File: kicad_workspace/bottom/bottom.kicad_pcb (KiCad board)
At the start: 4 copper layers, 76.8 x 84 mm, 75 parts, among them J1 691103110002, J2 BackupPad, J3 PROG_HEADER, J4 RPI_POWER_CONN, J5 UART_HEADER, J6 BackupPad, M1 N20_MOTOR_EXTENDED_SHAFT, M2 N20_MOTOR_EXTENDED_SHAFT, U1 DRV8833PWP, U12 ACS712-5A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

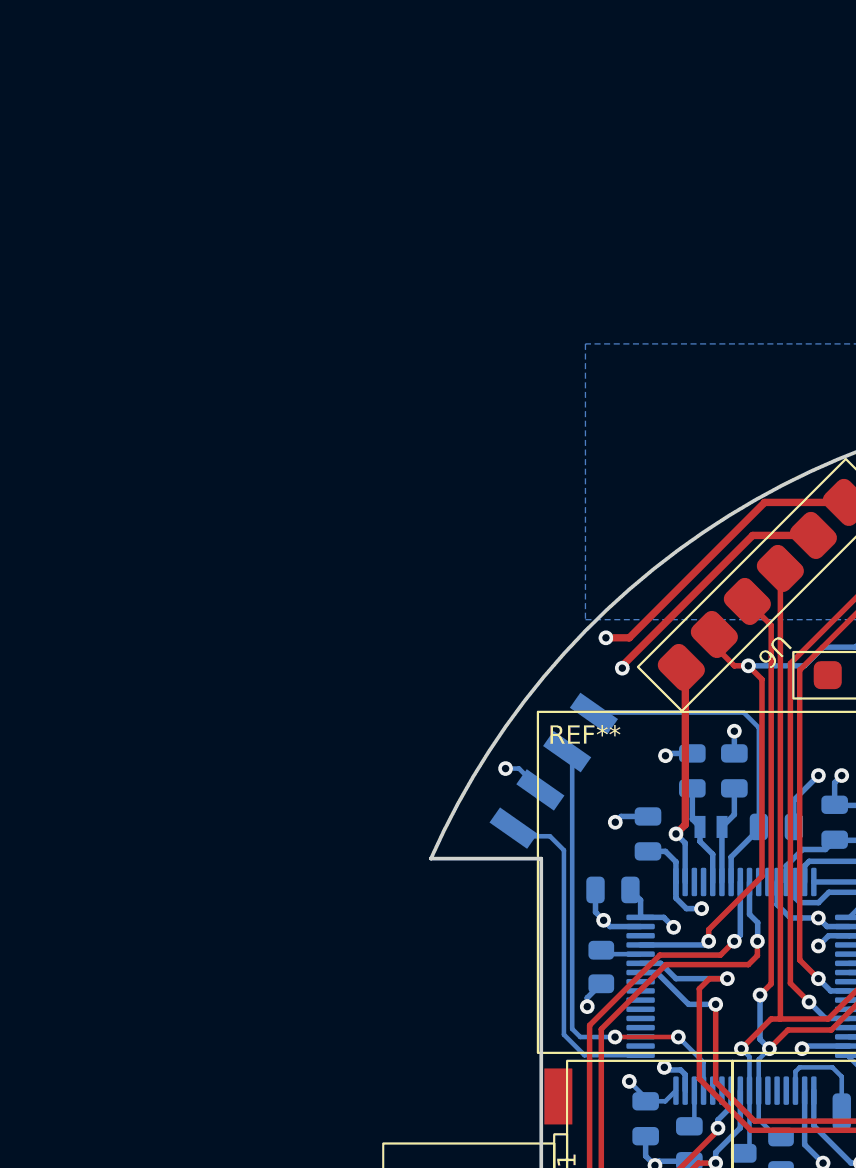
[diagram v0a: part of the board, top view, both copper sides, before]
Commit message: add 3.3v to programming header
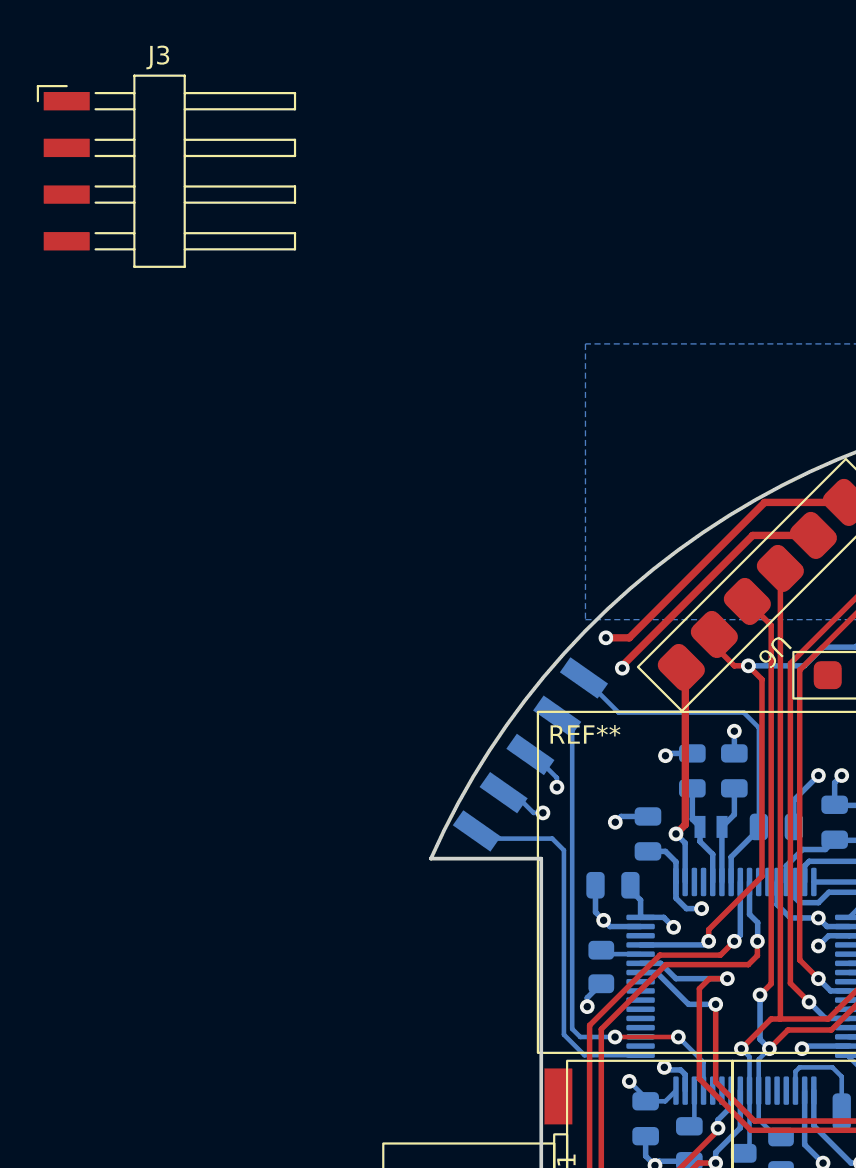
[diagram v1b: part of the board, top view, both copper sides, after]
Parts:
- added J7: Conn_01x05_Pin, Connector_Harwin:Harwin_M20-89005xx_1x05_P2.54mm_Horizontal, B.Cu at (22.5, 34.2)
- J3: moved to F.Cu
- moved J3 33.7 mm to (7.30, 5.61), turned to 0 degrees
- moved C11 0.25 mm to (31.5, 44.5)
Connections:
- J3 pad 1: NRST -> unconnected-(J3-Pin_1-Pad1)
- J3 pad 2: SWDIO -> unconnected-(J3-Pin_2-Pad2)
- J3 pad 3: -BATT_PROT -> unconnected-(J3-Pin_3-Pad3)
- J3 pad 4: SWCLK -> unconnected-(J3-Pin_4-Pad4)
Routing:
- net +3.3V: track 95.2 -> 97.8 mm, vias 21 -> 22
- net SWDIO: track 24.6 -> 26.8 mm
- net SWCLK: track 17.9 -> 19.8 mm
- net NRST: track 18.2 -> 19.5 mm

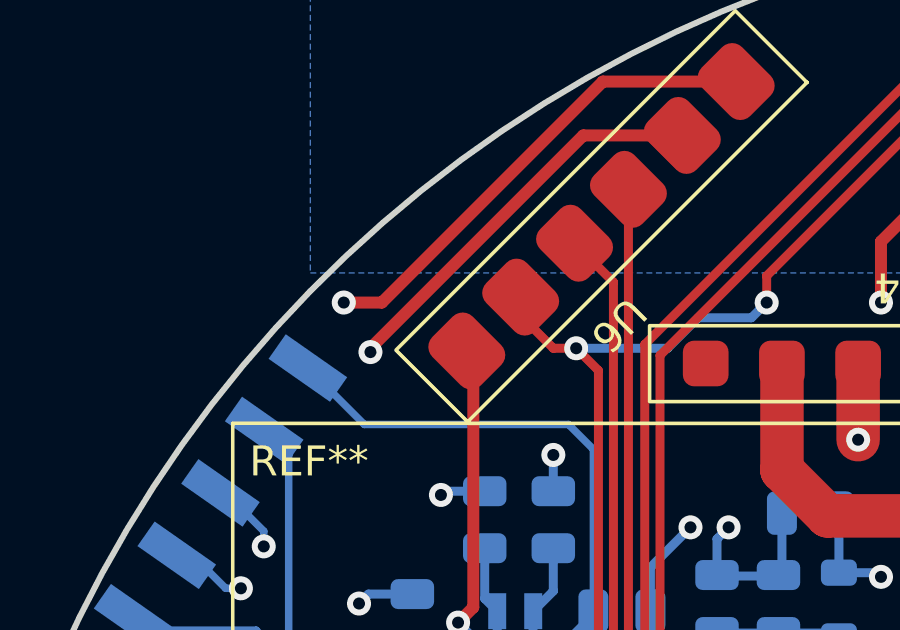
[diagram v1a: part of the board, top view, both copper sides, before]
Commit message: add text for charging pad+
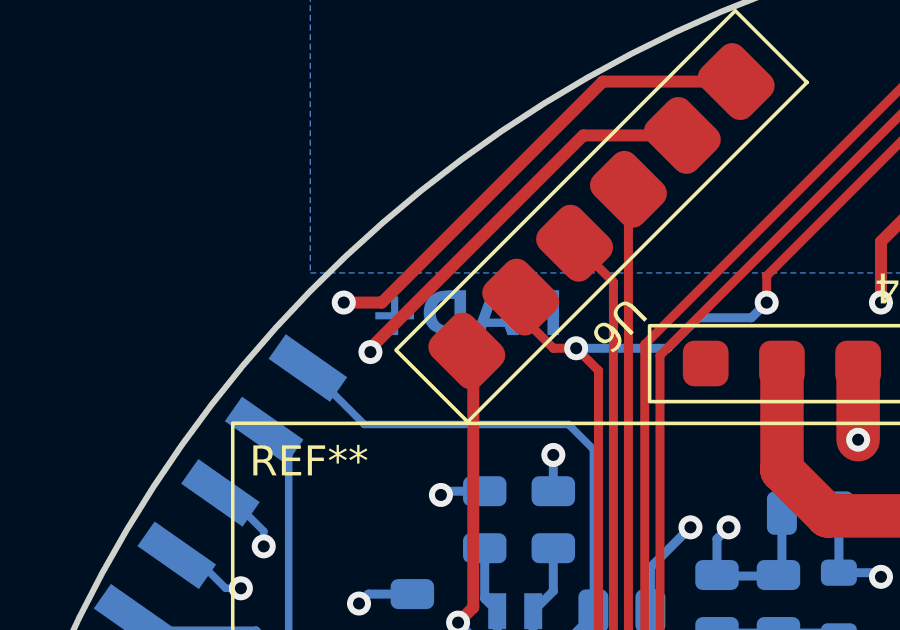
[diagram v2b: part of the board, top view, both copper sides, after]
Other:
- board text added: "PAD+"
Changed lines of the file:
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@@
   (gr_line (start 92.4057 43) (end 98.4057 43)
     (stroke (width 0.2) (type solid)) (layer "Edge.Cuts"))
+  (gr_text "PAD+" (at 38.481 32.258) (layer "B.Cu")
+    (effects (font (size 1.5 1.5) (thickness 0.3) bold) (justify left bottom mirror))
+  )
   (segment (start 57.655346 30.2035) (end 59.5855 30.2035) (width 0.254) (layer "F.Cu") (net 1))
   (segment (start 57.792846 28.9095) (end 58.086846 29.2035) (width 0.254) (layer "F.Cu") (net 1))

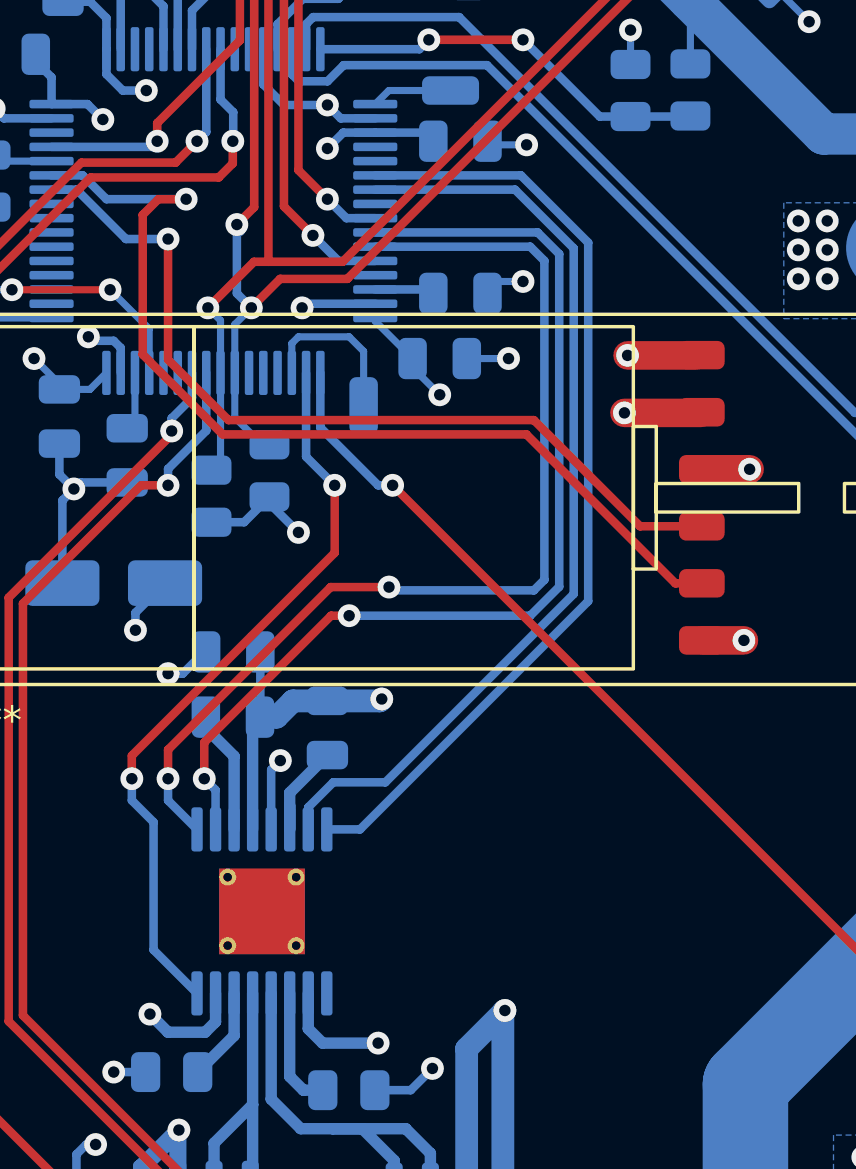
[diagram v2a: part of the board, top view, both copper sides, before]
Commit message: fix drv8833 wrong vint cap connection. connect nSleep pin to uC
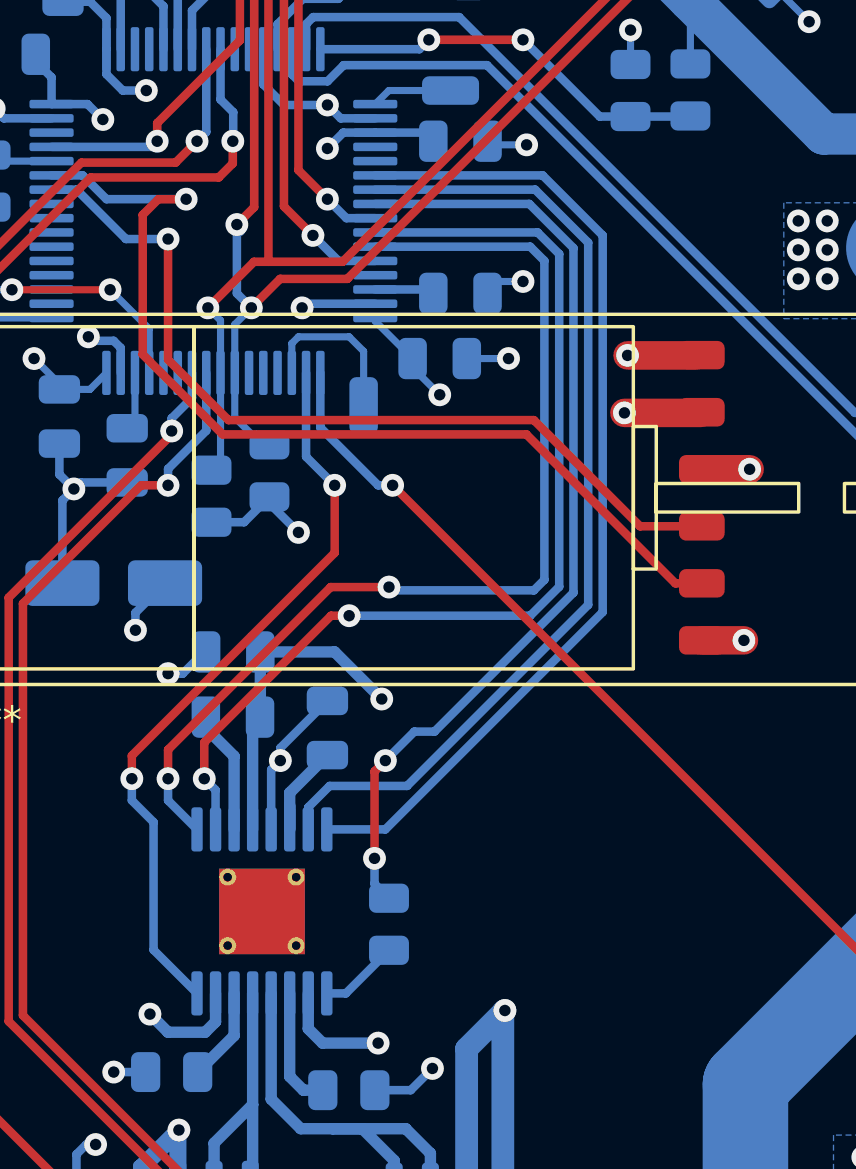
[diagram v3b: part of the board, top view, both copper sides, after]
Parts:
- added R16: 33K, Resistor_SMD:R_0805_2012Metric, B.Cu at (44.8, 75.0)
- C21: value 2.2uF -> 10uF
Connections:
- C20 pad 1: +5V -> -BATT_PROT
- U1 pad 1: DRV_SLEEP -> Net-(U1-nSLEEP)
- U17 pad 24: unconnected-(U17-PC4-Pad24) -> DRV_SLEEP
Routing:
- net DRV_SLEEP: track 0.00 -> 33.9 mm, vias 0 -> 2
- net Net-(U1-nSLEEP): track 0.00 -> 2.81 mm
- net -BATT_PROT: track 203.8 -> 206.5 mm
- net DRV_A1: track 33.5 -> 34.9 mm
- net DRV_A2: track 33.1 -> 34.5 mm

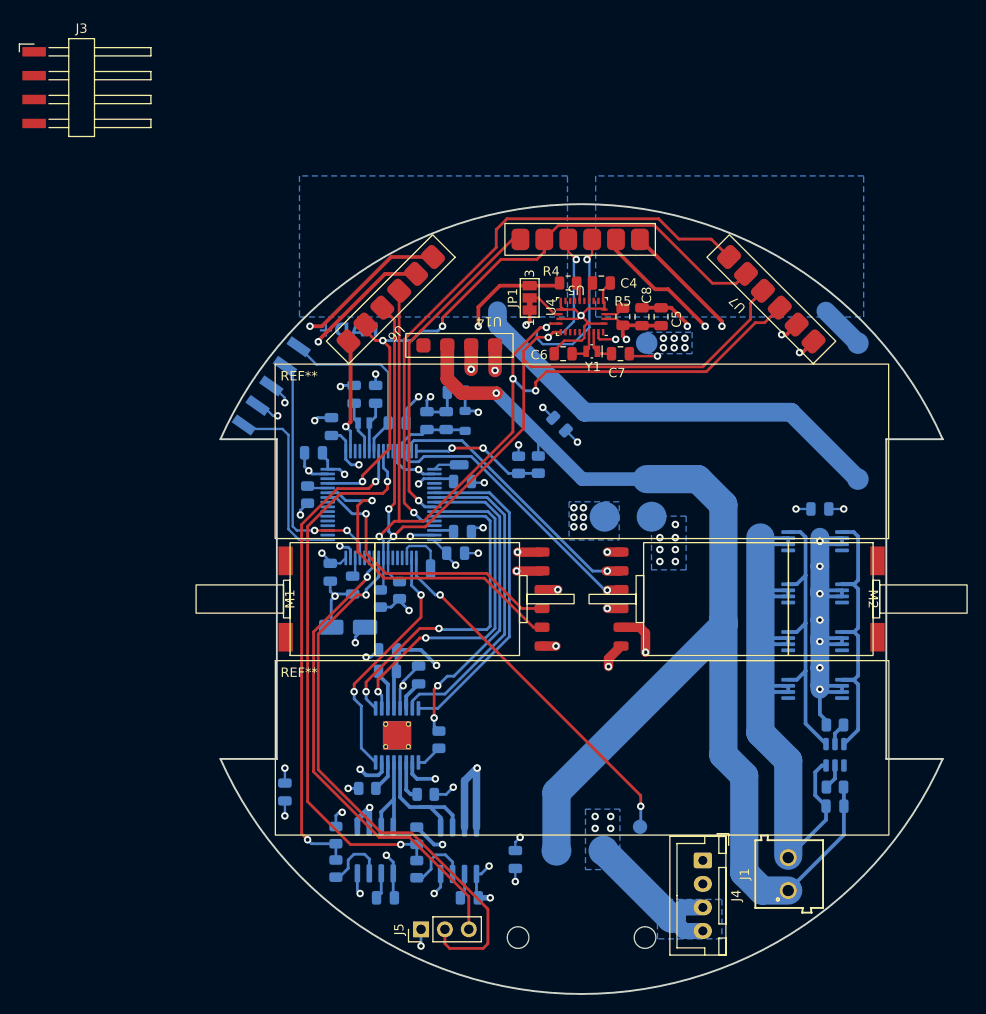
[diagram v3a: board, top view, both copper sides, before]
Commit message: change j4 power connector orientation
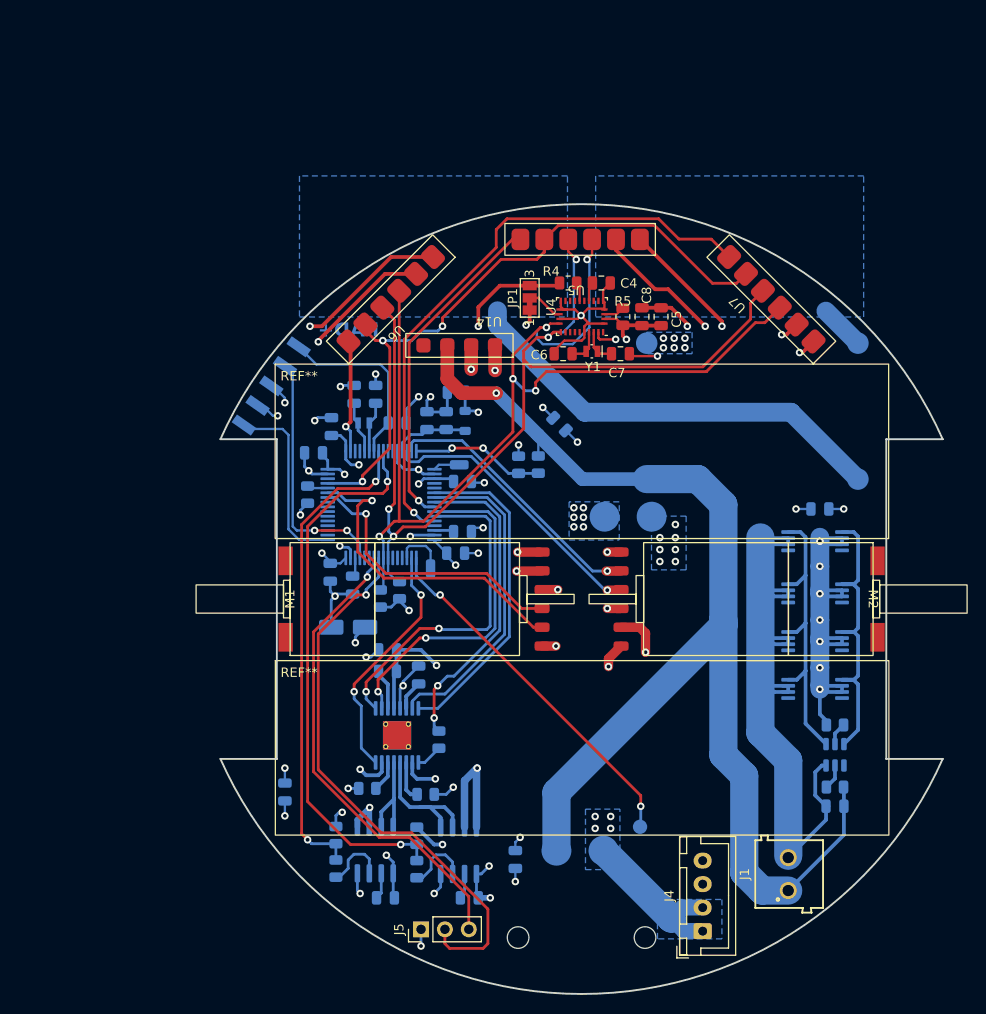
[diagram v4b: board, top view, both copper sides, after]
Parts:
- removed J3: PROG_HEADER, Connector_Harwin:Harwin_M20-89004xx_1x04_P2.54mm_Horizontal
- moved J4 7.52 mm to (72.9, 95.3), turned to 90 degrees
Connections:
- J4 pad 1: +5V -> -BATT_PROT
- J4 pad 2: +5V -> -BATT_PROT
- J4 pad 3: -BATT_PROT -> +5V
- J4 pad 4: -BATT_PROT -> +5V

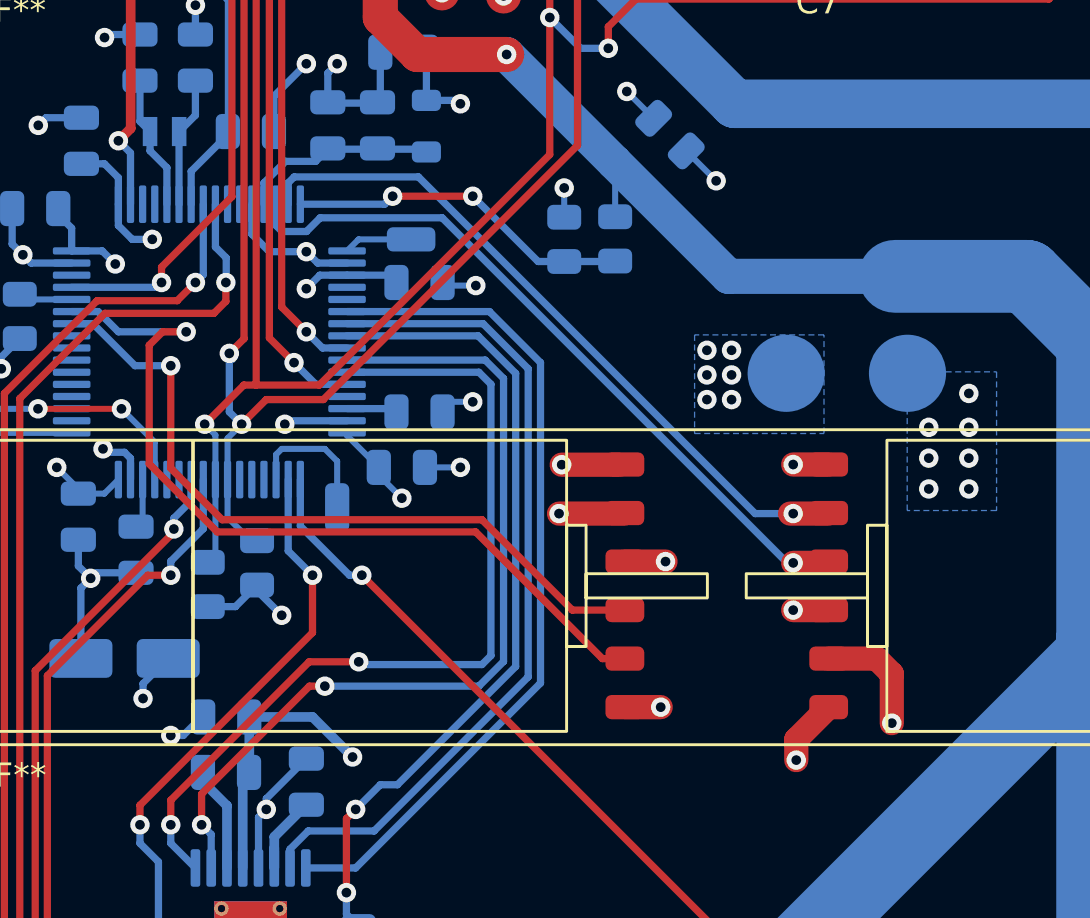
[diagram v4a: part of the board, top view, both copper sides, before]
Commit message: fix motors pinout
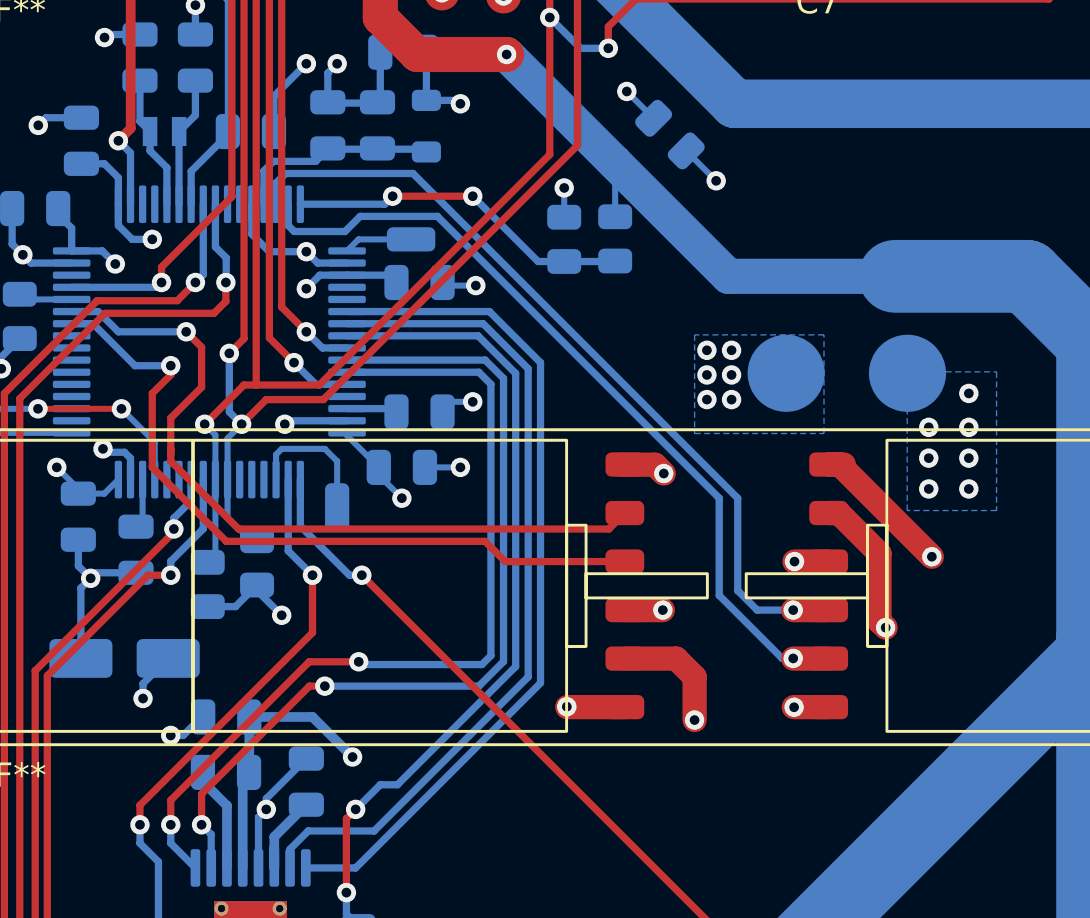
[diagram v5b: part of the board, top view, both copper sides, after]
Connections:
- M1 pad 1: -BATT_PROT -> /MOTOR_A-
- M1 pad 2: M1_B -> IP_MOTOR_A+
- M1 pad 3: M1_A -> +3.3V
- M1 pad 4: +3.3V -> M1_A
- M1 pad 5: IP_MOTOR_A+ -> M1_B
- M1 pad 6: /MOTOR_A- -> -BATT_PROT
- M2 pad 1: -BATT_PROT -> /MOTOR_B-
- M2 pad 2: M2_B -> IP_MOTOR_B+
- M2 pad 3: M2_A -> +3.3V
- M2 pad 4: +3.3V -> M2_A
- M2 pad 5: IP_MOTOR_B+ -> M2_B
- M2 pad 6: /MOTOR_B- -> -BATT_PROT
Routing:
- net /MOTOR_B-: track 41.3 -> 53.5 mm
- net IP_MOTOR_B+: track 48.6 -> 60.7 mm
- net /MOTOR_A-: track 34.7 -> 26.3 mm
- net M2_B: track 29.0 -> 33.4 mm
- net IP_MOTOR_A+: track 38.4 -> 34.6 mm
- net M2_A: track 29.9 -> 33.6 mm
- net M1_B: track 34.6 -> 31.6 mm
